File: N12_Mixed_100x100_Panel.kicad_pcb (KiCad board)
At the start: 2 copper layers, 100 x 100 mm, 80 parts, among them IC1 TJA1103AHN, J1 9-2304372-9 MATEnet, J1 Conn_02x02_Odd_Even, J2 2-Pin Wire Clamp, J2 Conn_02x11_Odd_Even, J3 9-2304372-9, J4 E6S20A-40MT5-Z, Q1 FDN340P, Q2 BSS138, SW1 SW_Push, SW2 SW-DIP-ANGLED DS03-254-02BE, SW2 SW_Push, SW3 SW_Push, SW4 SW_Push, SW5 SW_Push, SW6 SW_Push, U1 SeeeduinoXIAO, Y1 Crystal_GND24_Small

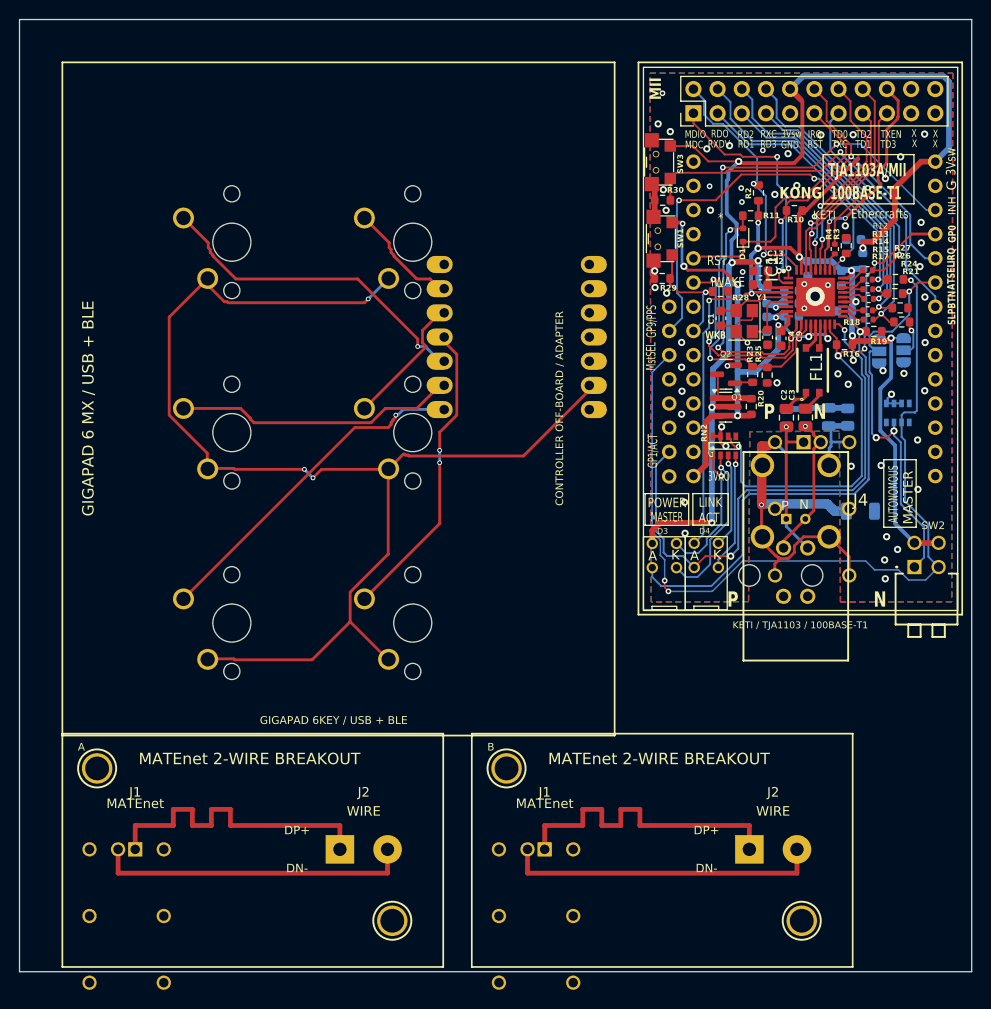
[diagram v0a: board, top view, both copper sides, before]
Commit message: finalize onboard ESP32 100x100 fabrication panel
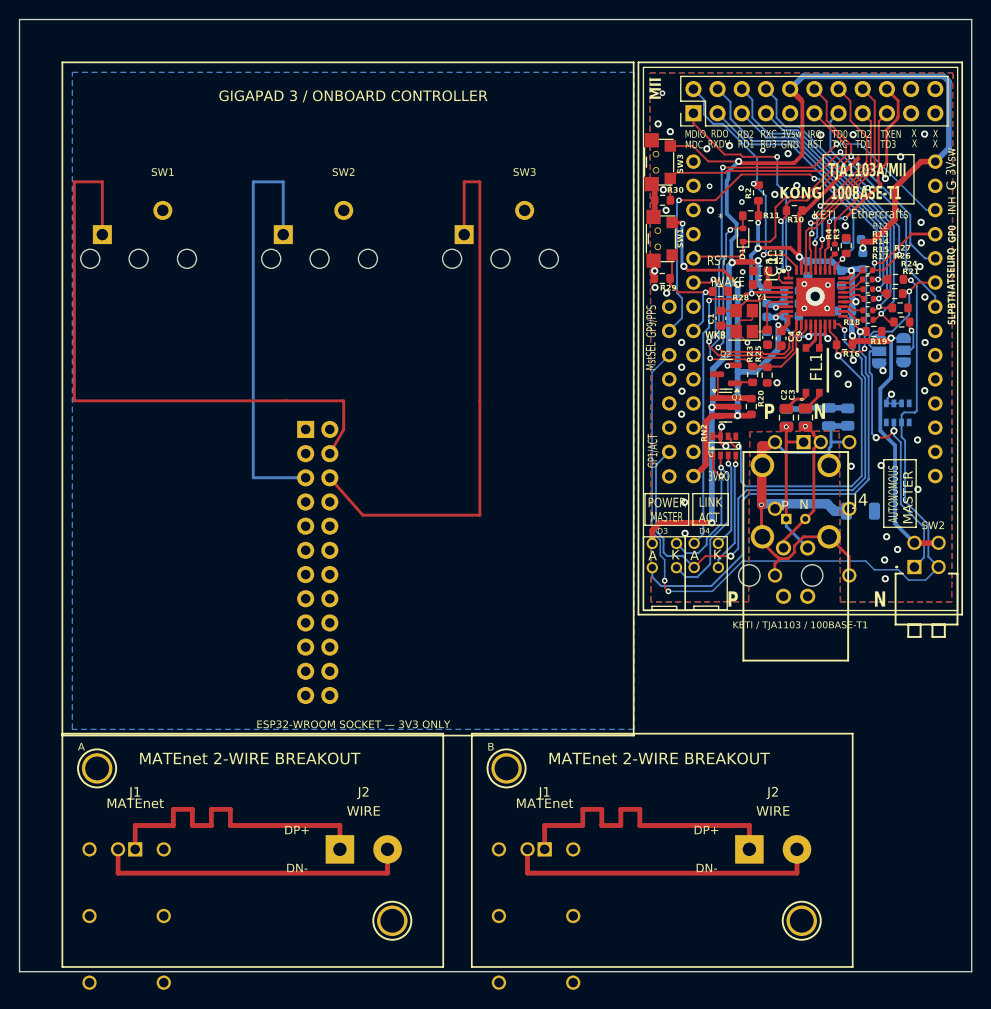
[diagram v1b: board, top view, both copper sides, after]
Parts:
- removed SW4, SW5, SW6: SW_Push, giga_pad_library:SW_Cherry_MX_1.00u_PCB
- SW1, SW2, SW3: value SW_Push -> (none); footprint giga_pad_library:SW_Cherry_MX_1.00u_PCB -> Cherry_MX_1u
- U1: value SeeeduinoXIAO -> ESP32-WROOM 3V3; footprint giga_pad_library:xiao-tht -> ESP32_WROOM_CARRIER_2x12_P2.54mm
- moved SW1 40.9 mm to (15.1, 20.1), turned to 0 degrees
- moved SW3 35.8 mm to (53.0, 20.1), turned to 0 degrees
- moved SW2 26.8 mm to (34.0, 20.1), turned to 0 degrees
- moved U1 24.2 mm to (30.1, 43.0)
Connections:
- net KETI_/ATNM1_MNGD0_SEL renamed /ATNM1_MNGD0_SEL
- net KETI_/CLK_IN_OUT25MHz renamed /CLK_IN_OUT25MHz
- net KETI_/DN- renamed /DN-
- net KETI_/DP+ renamed /DP+
- net KETI_/GP0/CONF0/nLINKLED renamed /GP0/CONF0/nLINKLED
- net KETI_/GP1/ACTLED renamed /GP1/ACTLED
- net KETI_/M1_S0_SELECT renamed /M1_S0_SELECT
- net KETI_/MDC renamed /MDC
- net KETI_/MDIO renamed /MDIO
- net KETI_/RXC/GP8 renamed /RXC/GP8
- net KETI_/RXD0/CONF5 renamed /RXD0/CONF5
- net KETI_/RXD1/CONF4 renamed /RXD1/CONF4
- net KETI_/RXD2/GP4/CONF3 renamed /RXD2/GP4/CONF3
- net KETI_/RXD3/GP3/CONF2 renamed /RXD3/GP3/CONF2
- net KETI_/RX_DV/CONF6 renamed /RX_DV/CONF6
- net KETI_/RX_ER/GP2/CONF1/ROLELED renamed /RX_ER/GP2/CONF1/ROLELED
- net KETI_/SleepBTN renamed /SleepBTN
- net KETI_/TRD+ renamed /TRD+
- net KETI_/TRD- renamed /TRD-
- net KETI_/TXC renamed /TXC
- net KETI_/TXD0 renamed /TXD0
- net KETI_/TXD1 renamed /TXD1
- net KETI_/TXD2/GP10 renamed /TXD2/GP10
- net KETI_/TXD3/GP11 renamed /TXD3/GP11
- net KETI_/TX_EN renamed /TX_EN
- net KETI_/TX_ER/GP9/oPPS renamed /TX_ER/GP9/oPPS
- net KETI_/VDD_CORE renamed /VDD_CORE
- net KETI_/WAKEBTN renamed /WAKEBTN
- net KETI_/XI renamed /XI
- net KETI_/XO renamed /XO
- net KETI_/iWAKE renamed /iWAKE
- net KETI_/nINHLED renamed /nINHLED
- net KETI_/nIRQ renamed /nIRQ
- net KETI_/nRST renamed /nRST
- net KETI_/nRST/SYS renamed /nRST/SYS
- net KETI_/oINH renamed /oINH
- net KETI_Earth renamed Earth
- net KETI_Net-(C2-Pad2) renamed Net-(C2-Pad2)
- net KETI_Net-(C3-Pad2) renamed Net-(C3-Pad2)
- net KETI_Net-(C6-Pad2) renamed Net-(C6-Pad2)
- net KETI_Net-(D3-K1) renamed Net-(D3-K1)
- net KETI_Net-(D3-K2) renamed Net-(D3-K2)
- net KETI_Net-(D4-K1) renamed Net-(D4-K1)
- net KETI_Net-(D4-K2) renamed Net-(D4-K2)
- net KETI_Net-(IC1-RXC/GP8/TX_TCLK) renamed Net-(IC1-RXC/GP8/TX_TCLK)
- net KETI_Net-(IC1-RXD0/CONF5) renamed Net-(IC1-RXD0/CONF5)
- net KETI_Net-(IC1-RXD1/CONF4) renamed Net-(IC1-RXD1/CONF4)
- net KETI_Net-(IC1-RXD2/GP4/CONF3) renamed Net-(IC1-RXD2/GP4/CONF3)
- net KETI_Net-(IC1-RXD3/GP3/CONF2) renamed Net-(IC1-RXD3/GP3/CONF2)
- net KETI_Net-(IC1-RX_DV/RXCTL/CONF6) renamed Net-(IC1-RX_DV/RXCTL/CONF6)
- net KETI_Net-(IC1-TXC) renamed Net-(IC1-TXC)
- net KETI_Net-(JP1-C) renamed Net-(JP1-C)
- net KETI_Net-(Q2-G) renamed Net-(Q2-G)
- net KETI_VDD3V3cont renamed VDD3V3cont
- net KETI_VDD3V3sw renamed VDD3V3sw
- net KETI_VDDD3V3 renamed VDDD3V3
- net KETI_VREGA_IN renamed VREGA_IN
- net KETI_VREGA_OUT renamed VREGA_OUT
- C1 pad 2: KETI_GND -> GND
- C12 pad 2: KETI_GND -> GND
- C13 pad 2: KETI_GND -> GND
- C14 pad 2: KETI_GND -> GND
- C15 pad 2: KETI_GND -> GND
- C16 pad 2: KETI_GND -> GND
- C17 pad 2: KETI_GND -> GND
- C18 pad 2: KETI_GND -> GND
- C20 pad 2: KETI_GND -> GND
- C21 pad 2: KETI_GND -> GND
- C4 pad 2: KETI_GND -> GND
- C7 pad 1: KETI_GND -> GND
- C8 pad 2: KETI_GND -> GND
- C9 pad 2: KETI_GND -> GND
- IC1 pad 37: KETI_GND -> GND
- J1 pad 1: DONGLE_B_MATENET_DP+ -> MATENET_DP+
- J1 pad 2: DONGLE_B_MATENET_DN- -> MATENET_DN-
- J1 pad 1: DONGLE_A_MATENET_DP+ -> MATENET_DP+
- J1 pad 2: DONGLE_A_MATENET_DN- -> MATENET_DN-
- J1 pad 1: KETI_unconnected-(J1-Pin_1-Pad1) -> unconnected-(J1-Pin_1-Pad1)
- J1 pad 3: KETI_unconnected-(J1-Pin_3-Pad3) -> unconnected-(J1-Pin_3-Pad3)
- J2 pad 1: DONGLE_A_MATENET_DP+ -> MATENET_DP+
- J2 pad 2: DONGLE_A_MATENET_DN- -> MATENET_DN-
- J2 pad 1: DONGLE_B_MATENET_DP+ -> MATENET_DP+
- J2 pad 2: DONGLE_B_MATENET_DN- -> MATENET_DN-
- J2 pad 20: KETI_unconnected-(J2-Pin_20-Pad20) -> unconnected-(J2-Pin_20-Pad20)
- J2 pad 21: KETI_unconnected-(J2-Pin_21-Pad21) -> unconnected-(J2-Pin_21-Pad21)
- J2 pad 22: KETI_unconnected-(J2-Pin_22-Pad22) -> unconnected-(J2-Pin_22-Pad22)
- J2 pad 9: KETI_GND -> GND
- JP1 pad 3: KETI_GND -> GND
- JP2 pad 3: KETI_GND -> GND
- Q2 pad 2: KETI_GND -> GND
- R19 pad 1: KETI_GND -> GND
- R24 pad 1: KETI_GND -> GND
- R25 pad 1: KETI_GND -> GND
- R29 pad 2: KETI_GND -> GND
- R3 pad 2: KETI_GND -> GND
- R30 pad 1: KETI_GND -> GND
- RN1 pad 1: KETI_GND -> GND
- RN1 pad 2: KETI_GND -> GND
- RN1 pad 3: KETI_GND -> GND
- RN1 pad 4: KETI_unconnected-(RN1-R4.1-Pad4) -> unconnected-(RN1-R4.1-Pad4)
- RN1 pad 5: KETI_unconnected-(RN1-R4.2-Pad5) -> unconnected-(RN1-R4.2-Pad5)
- RN1 pad 8: KETI_unconnected-(RN1-R1.2-Pad8) -> unconnected-(RN1-R1.2-Pad8)
- RN2 pad 5: KETI_GND -> GND
- RN2 pad 7: KETI_GND -> GND
- RN2 pad 8: KETI_GND -> GND
- SW1 pad 3: KETI_GND -> GND
- SW1 pad 4: KETI_GND -> GND
- SW1 pad 5: KETI_unconnected-(SW1-Pad5) -> unconnected-(SW1-Pad5)
- SW1 pad 6: KETI_unconnected-(SW1-Pad6) -> unconnected-(SW1-Pad6)
- SW3 pad 3: KETI_GND -> GND
- SW3 pad 4: KETI_GND -> GND
- SW3 pad 5: KETI_unconnected-(SW3-Pad5) -> unconnected-(SW3-Pad5)
- SW3 pad 6: KETI_unconnected-(SW3-Pad6) -> unconnected-(SW3-Pad6)
- U1 pad 1: KETI_unconnected-(U1-CANRX-Pad1) -> unconnected-(U1-CANRX-Pad1)
- U1 pad 13: KETI_GND -> GND
- U1 pad 15: KETI_unconnected-(U1-nCS-Pad15) -> unconnected-(U1-nCS-Pad15)
- U1 pad 16: KETI_unconnected-(U1-SCLK-Pad16) -> unconnected-(U1-SCLK-Pad16)
- U1 pad 17: KETI_unconnected-(U1-MOSI-Pad17) -> unconnected-(U1-MOSI-Pad17)
- U1 pad 18: KETI_unconnected-(U1-MISO-Pad18) -> unconnected-(U1-MISO-Pad18)
- U1 pad 2: KETI_unconnected-(U1-CANTX-Pad2) -> unconnected-(U1-CANTX-Pad2)
- U1 pad 21: KETI_unconnected-(U1-GP21-Pad21) -> unconnected-(U1-GP21-Pad21)
- U1 pad 23: KETI_unconnected-(U1-SCL-Pad23) -> unconnected-(U1-SCL-Pad23)
- U1 pad 24: KETI_unconnected-(U1-SDA-Pad24) -> unconnected-(U1-SDA-Pad24)
- U1 pad 25: KETI_unconnected-(U1-UBTX-Pad25) -> unconnected-(U1-UBTX-Pad25)
- U1 pad 26: KETI_unconnected-(U1-UBRX-Pad26) -> unconnected-(U1-UBRX-Pad26)
- U1 pad 27: KETI_GND -> GND
- U1 pad 29: KETI_unconnected-(U1-5V-Pad29) -> unconnected-(U1-5V-Pad29)
- U1 pad 3: KETI_unconnected-(U1-LINEN-Pad3) -> unconnected-(U1-LINEN-Pad3)
- U1 pad 31: KETI_unconnected-(U1-GP31-Pad31) -> unconnected-(U1-GP31-Pad31)
- U1 pad 32: KETI_unconnected-(U1-GP32-Pad32) -> unconnected-(U1-GP32-Pad32)
- U1 pad 33: KETI_unconnected-(U1-GP33-Pad33) -> unconnected-(U1-GP33-Pad33)
- U1 pad 36: KETI_unconnected-(U1-GP36-Pad36) -> unconnected-(U1-GP36-Pad36)
- U1 pad 4: KETI_unconnected-(U1-PPS-Pad4) -> unconnected-(U1-PPS-Pad4)
- U1 pad 5: KETI_unconnected-(U1-Pad5) -> unconnected-(U1-Pad5)
- U1 pad 6: KETI_unconnected-(U1-Pad6) -> unconnected-(U1-Pad6)
- U1 pad 7: KETI_unconnected-(U1-nCS1-Pad7) -> unconnected-(U1-nCS1-Pad7)
- U1 pad 1: SW_1 -> 3V3
- U1 pad 10: (no net) -> GND
- U1 pad 13: GND -> (no net)
- U1 pad 2: SW_2 -> 5V
- U1 pad 3: SW_3 -> GND
- U1 pad 4: SW_4 -> SW_1
- U1 pad 5: SW_5 -> SW_2
- U1 pad 6: SW_6 -> SW_3
- U1 pad 7: (no net) -> UART_TX
- U1 pad 8: (no net) -> UART_RX
- U1 pad 9: (no net) -> GND
- Y1 pad 2: KETI_GND -> GND
- Y1 pad 4: KETI_GND -> GND
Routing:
- net GND: track 230.0 -> 100.6 mm, vias 4 -> 50
- net SW_1: track 37.8 -> 134.6 mm, vias 1 -> 0
- net /RXD3/GP3/CONF2: track 91.5 -> 3.21 mm, vias 3 -> 1
- net Net-(IC1-RXD3/GP3/CONF2): track 28.8 -> 91.5 mm, vias 1 -> 3
- net SW_2: track 98.1 -> 47.8 mm
- net SW_4: track 47.4 -> 0.00 mm, vias 3 -> 0
- net unconnected-(U1-CANRX-Pad1): track 0.00 -> 41.8 mm, vias 0 -> 1
- net KETI_unconnected-(U1-CANRX-Pad1): track 41.8 -> 0.00 mm, vias 1 -> 0
- net unconnected-(U1-UBRX-Pad26): track 0.00 -> 28.5 mm, vias 0 -> 1
- net KETI_unconnected-(U1-UBRX-Pad26): track 28.5 -> 0.00 mm, vias 1 -> 0
- net unconnected-(U1-UBTX-Pad25): track 0.00 -> 27.6 mm, vias 0 -> 1
- net KETI_unconnected-(U1-UBTX-Pad25): track 27.6 -> 0.00 mm, vias 1 -> 0
- net /RXD2/GP4/CONF3: track 2.43 -> 28.8 mm, vias 0 -> 1
- net SW_3: track 65.0 -> 90.6 mm, vias 2 -> 1
- net UART_RX: track 0.00 -> 20.3 mm, vias 0 -> 12
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- added copper zone on B.Cu, net GND
- added copper zone on F.Cu, net GND
- removed copper zone on B.Cu, net KETI_GND
- removed copper zone on F.Cu, net KETI_GND
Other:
- board text added: "ESP32-WROOM SOCKET — 3V3 ONLY"
- board text added: "GIGAPAD 3 / ONBOARD CONTROLLER"
- board text removed: "CONTROLLER OFF-BOARD / ADAPTER"
- board text removed: "GIGAPAD 6 MX / USB + BLE"
- board text removed: "GIGAPAD 6KEY / USB + BLE"
